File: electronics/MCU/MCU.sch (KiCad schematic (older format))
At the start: 42 parts, among them J1 UART, J10 Conn_01x09, J11 Button, J12 Power, J2 Conn_01x01, J3 Conn_01x01, J4 Conn_01x01, J5 Conn_01x01, J6 Conn_01x01, J7 Conn_01x01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

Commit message: Relay board ready, ESP3266 redesign (GPIO16 instead of GPIO0)
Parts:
- removed C2: 100n, Capacitor_SMD:C_1206_3216Metric_Pad1.42x1.75mm_HandSolder, symbol Device:C_Small
- removed SW1: Flash, Button_Switch_SMD:SW_SPST_SKQG_WithStem, symbol Switch:SW_Push
- R13: value 1k -> 10k
- R3: value 10k -> 3.3k
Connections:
- net GPIO0: now also J11.2 (Pin_2); no longer Q2.1 (G)
- net RST: now reaches R1.2, SW2.1, U1.1 (REST)
- net GPIO16: now reaches R13.2, U1.4 (GPIO16)
- net GPIO16: now also Q2.1 (G); no longer J11.2 (Pin_2)
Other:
- moved on the sheet: J11, J5, Q5, R1, R13, R2, R8, SW2

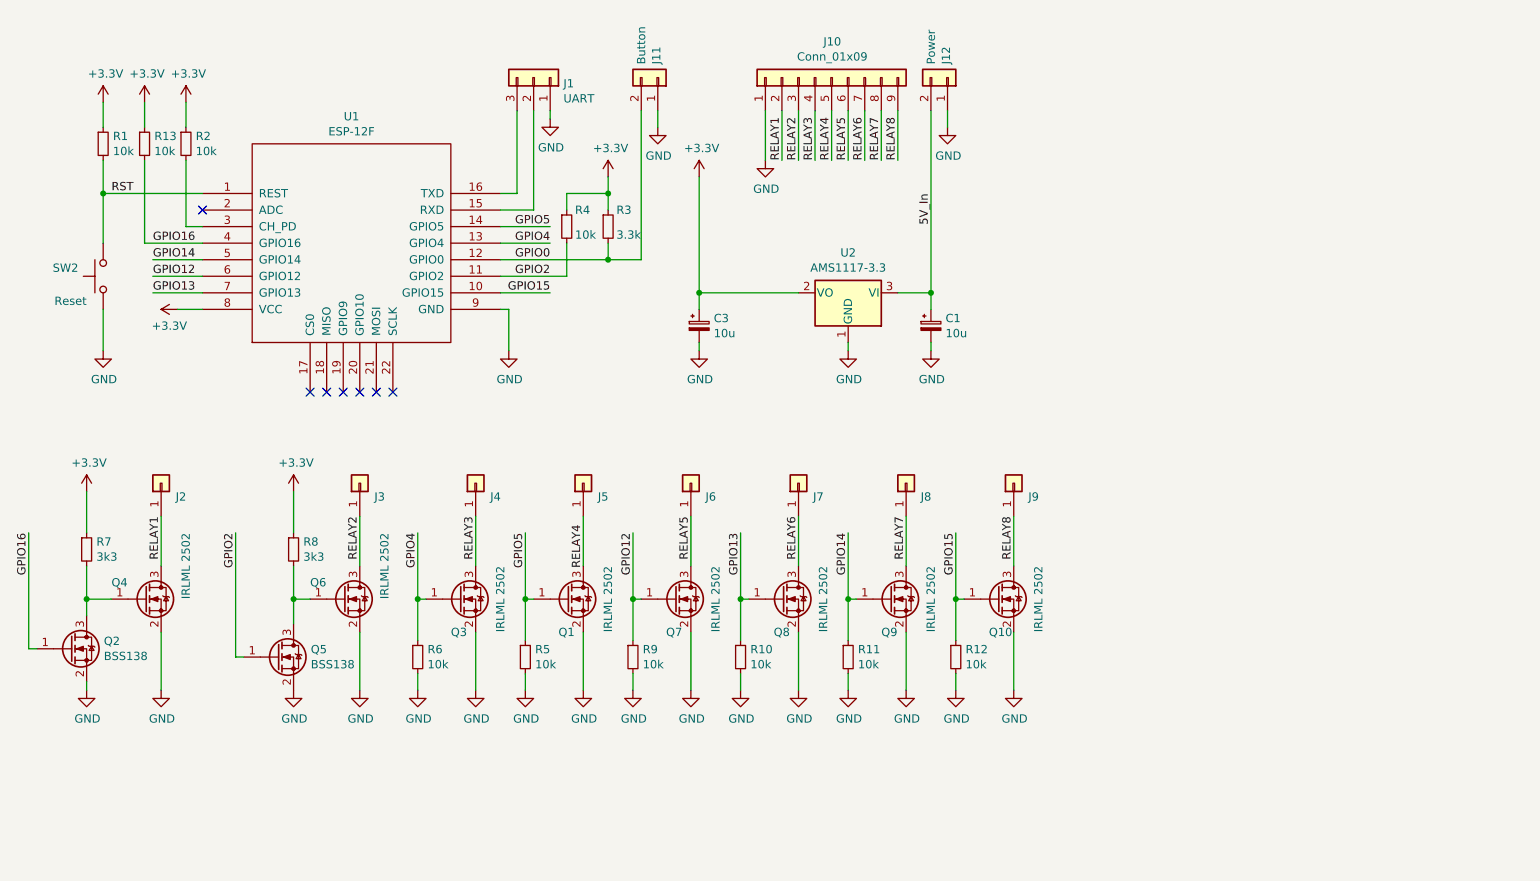
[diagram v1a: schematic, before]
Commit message: MCU: GPIO3 instead if GPIO2
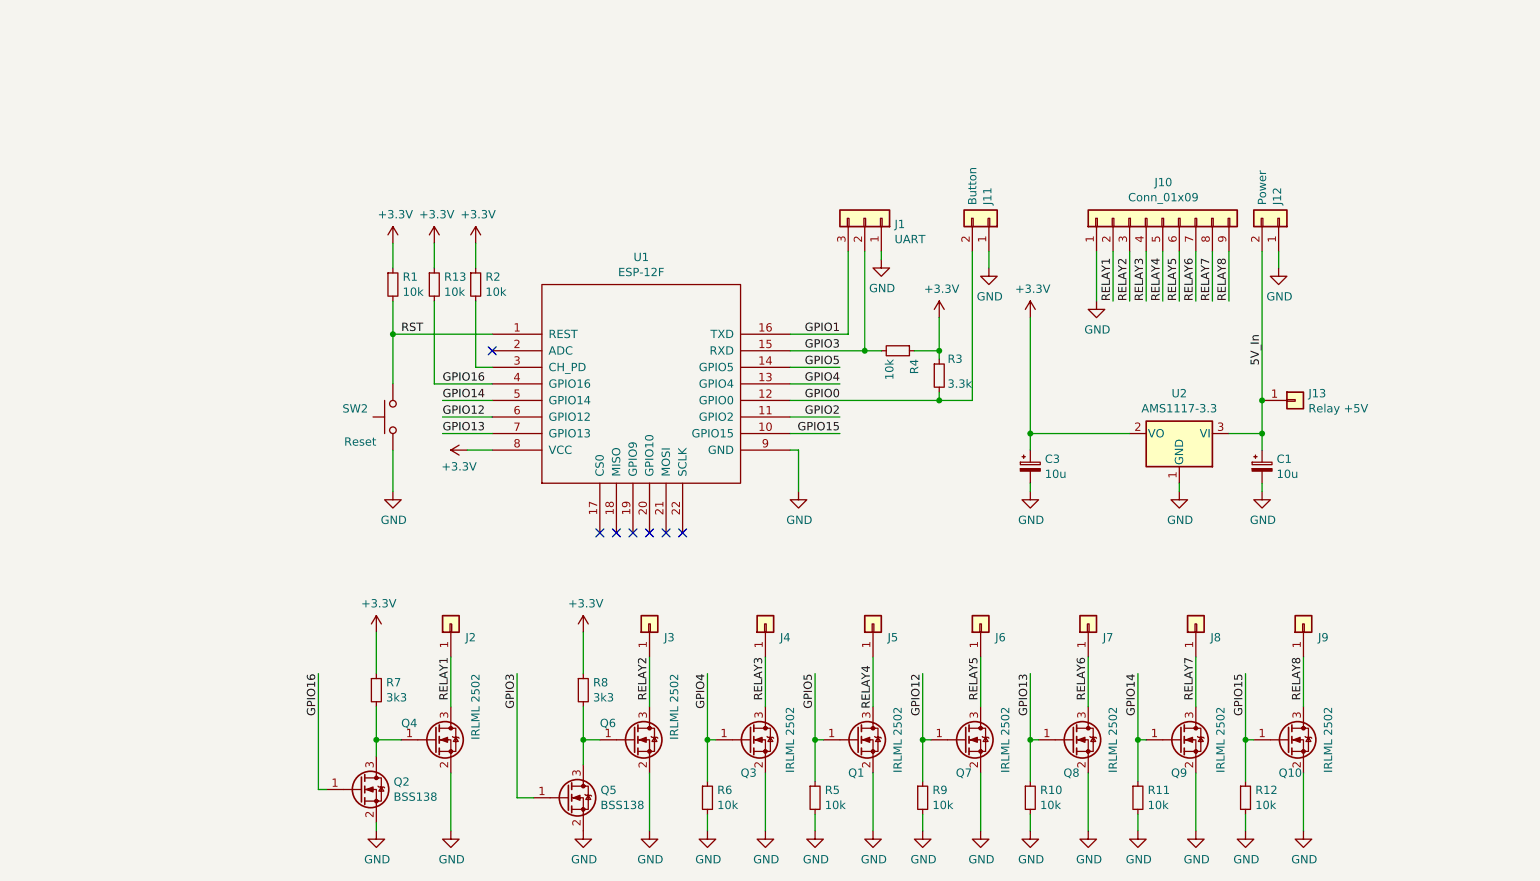
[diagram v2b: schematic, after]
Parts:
- added J13: Relay +5V, Connector_Wire:SolderWire-0.5sqmm_1x01_D0.9mm_OD2.1mm, symbol Connector_Generic:Conn_01x01
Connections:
- net 5V_In: now also J13.1 (Pin_1)
- net GPIO2: no longer Q5.1 (G), R4.2
- net GPIO3: now reaches J1.2 (Pin_2), U1.15 (RXD)
- net GPIO3: now also Q5.1 (G), R4.2
- net GPIO1: now reaches J1.3 (Pin_3), U1.16 (TXD)
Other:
- moved on the sheet: C1, C3, J1, J10, J11, J12, J2, J3, J4, J5, J6, J7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

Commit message: Small PCB modifications, esphome config added
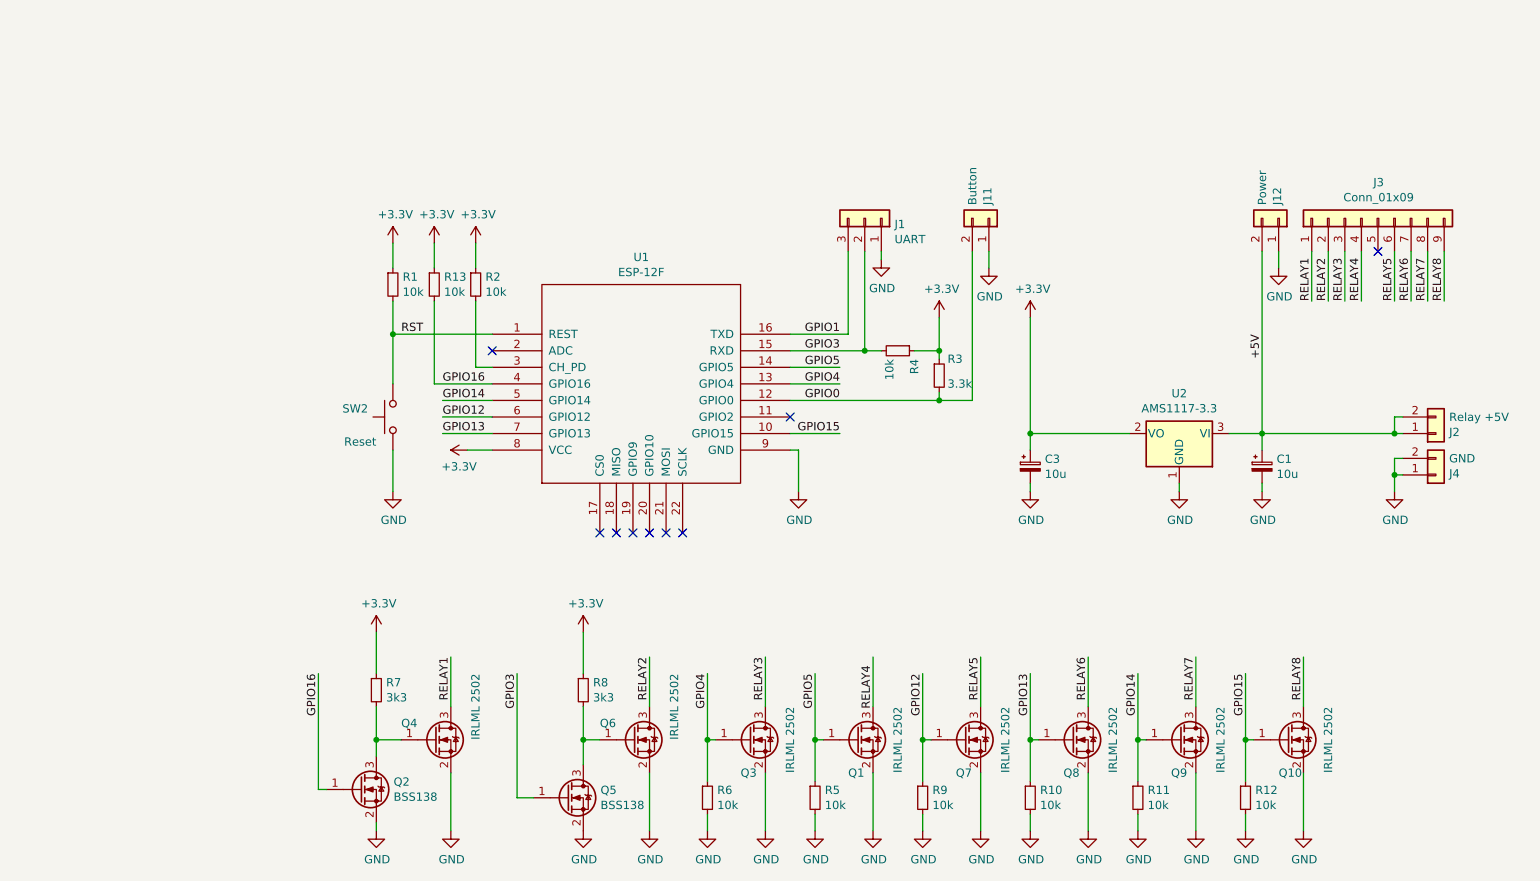
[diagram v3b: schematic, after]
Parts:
- removed J10: Conn_01x09, Connector_PinHeader_2.54mm:PinHeader_1x09_P2.54mm_Vertical, symbol Connector_Generic:Conn_01x09
- removed J13: Relay +5V, Connector_Wire:SolderWire-0.5sqmm_1x01_D0.9mm_OD2.1mm, symbol Connector_Generic:Conn_01x01
- removed J2, J3, J4, J5, J6, J7, J8, J9: Conn_01x01, Connector_Wire:SolderWirePad_1x01_SMD_1x2mm, symbol Connector_Generic:Conn_01x01
- added J2: Relay +5V, Connector_PinHeader_2.54mm:PinHeader_1x02_P2.54mm_Vertical, symbol Connector_Generic:Conn_01x02
- added J3: Conn_01x09, Connector_PinHeader_2.54mm:PinHeader_1x09_P2.54mm_Vertical, symbol Connector_Generic:Conn_01x09
- added J4: GND, Connector_PinHeader_2.54mm:PinHeader_1x02_P2.54mm_Vertical, symbol Connector_Generic:Conn_01x02
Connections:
- net GND: now also J4.1 (Pin_1), J4.2 (Pin_2)
- net RELAY1: now also J3.1 (Pin_1)
- net RELAY2: now also J3.2 (Pin_2)
- net RELAY3: now also J3.3 (Pin_3)
- net RELAY4: now also J3.4 (Pin_4)
- net RELAY5: now also J3.6 (Pin_6)
- net RELAY6: now also J3.7 (Pin_7)
- net RELAY7: now also J3.8 (Pin_8)
- net RELAY8: now also J3.9 (Pin_9)
- net 5V_In renamed +5V
- net +5V: now also J2.1 (Pin_1), J2.2 (Pin_2)
- net GPIO2: no longer names the net of U1.11 (GPIO2)
- no-connect marks 7 -> 9
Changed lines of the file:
@@
 Wire Wire Line
 	5200 2850 6100 2850
-Text Label 5500 2850 2    50   ~ 0
-GPIO0
 $Comp
 L Device:R_Small R7
@@
 Text Label 4350 4400 3    50   ~ 0
 RELAY2
-Text Label 5500 2950 2    50   ~ 0
-GPIO2
 $Comp
 L power:GND #PWR0107
@@
 	1    0    0    -1
 $EndComp
-$Comp
-L Connector_Generic:Conn_01x01 J2
-U 1 1 608085B0
-P 3150 4200
-F 0 "J2" V 3068 4112 50  0000 R CNN
-F 1 "Conn_01x01" V 3023 4112 50  0001 R CNN
-F 2 "Connector_Wire:SolderWirePad_1x01_SMD_1x2mm" H 3150 4200 50  0001 C CNN
-F 3 "~" H 3150 4200 50  0001 C CNN
-	1    3150 4200
-	0    -1   -1   0
-$EndComp
 Wire Wire Line
 	4350 4700 4350 4400
-$Comp
-L Connector_Generic:Conn_01x01 J3
-U 1 1 60809E77
-P 4350 4200
-F 0 "J3" V 4268 4112 50  0000 R CNN
-F 1 "Conn_01x01" V 4223 4112 50  0001 R CNN
-F 2 "Connector_Wire:SolderWirePad_1x01_SMD_1x2mm" H 4350 4200 50  0001 C CNN
-F 3 "~" H 4350 4200 50  0001 C CNN
-	1    4350 4200
-	0    -1   -1   0
-$EndComp
-$Comp
-L Connector_Generic:Conn_01x01 J4
-U 1 1 6080A4B7
-P 5050 4200
-F 0 "J4" V 4968 4112 50  0000 R CNN
-F 1 "Conn_01x01" V 4923 4112 50  0001 R CNN
-F 2 "Connector_Wire:SolderWirePad_1x01_SMD_1x2mm" H 5050 4200 50  0001 C CNN
-F 3 "~" H 5050 4200 50  0001 C CNN
-	1    5050 4200
-	0    -1   -1   0
-$EndComp
-$Comp
-L Connector_Generic:Conn_01x01 J5
-U 1 1 6080AAE4
-P 5700 4200
-F 0 "J5" V 5618 4112 50  0000 R CNN
-F 1 "Conn_01x01" V 5573 4112 50  0001 R CNN
-F 2 "Connector_Wire:SolderWirePad_1x01_SMD_1x2mm" H 5700 4200 50  0001 C CNN
-F 3 "~" H 5700 4200 50  0001 C CNN
-	1    5700 4200
-	0    -1   -1   0
-$EndComp
-$Comp
-L Connector_Generic:Conn_01x01 J6
-U 1 1 6080B190
-P 6350 4200
-F 0 "J6" V 6268 4112 50  0000 R CNN
-F 1 "Conn_01x01" V 6223 4112 50  0001 R CNN
-F 2 "Connector_Wire:SolderWirePad_1x01_SMD_1x2mm" H 6350 4200 50  0001 C CNN
-F 3 "~" H 6350 4200 50  0001 C CNN
-	1    6350 4200
-	0    -1   -1   0
-$EndComp
-$Comp
-L Connector_Generic:Conn_01x01 J7
-U 1 1 6080B814
-P 7000 4200
-F 0 "J7" V 6918 4112 50  0000 R CNN
-F 1 "Conn_01x01" V 6873 4112 50  0001 R CNN
-F 2 "Connector_Wire:SolderWirePad_1x01_SMD_1x2mm" H 7000 4200 50  0001 C CNN
-F 3 "~" H 7000 4200 50  0001 C CNN
-	1    7000 4200
-	0    -1   -1   0
-$EndComp
-$Comp
-L Connector_Generic:Conn_01x01 J8
-U 1 1 6080BE94
-P 7650 4200
-F 0 "J8" V 7568 4112 50  0000 R CNN
-F 1 "Conn_01x01" V 7523 4112 50  0001 R CNN
-F 2 "Connector_Wire:SolderWirePad_1x01_SMD_1x2mm" H 7650 4200 50  0001 C CNN
-F 3 "~" H 7650 4200 50  0001 C CNN
-	1    7650 4200
-	0    -1   -1   0
-$EndComp
-$Comp
-L Connector_Generic:Conn_01x01 J9
-U 1 1 6080C4EB
-P 8300 4200
-F 0 "J9" V 8218 4112 50  0000 R CNN
-F 1 "Conn_01x01" V 8173 4112 50  0001 R CNN
-F 2 "Connector_Wire:SolderWirePad_1x01_SMD_1x2mm" H 8300 4200 50  0001 C CNN
-F 3 "~" H 8300 4200 50  0001 C CNN
-	1    8300 4200
-	0    -1   -1   0
-$EndComp
-$Comp
-L Connector_Generic:Conn_01x09 J10
-U 1 1 60824243
-P 7450 1750
-F 0 "J10" V 7667 1746 50  0000 C CNN
-F 1 "Conn_01x09" V 7576 1746 50  0000 C CNN
-F 2 "Connector_PinHeader_2.54mm:PinHeader_1x09_P2.54mm_Vertical" H 7450 1750 50  0001 C CNN
-F 3 "~" H 7450 1750 50  0001 C CNN
-	1    7450 1750
-	0    -1   -1   0
-$EndComp
-Wire Wire Line
-	7050 1950 7050 2250
-Wire Wire Line
-	7150 1950 7150 2250
-Wire Wire Line
-	7250 1950 7250 2250
-Wire Wire Line
-	7350 1950 7350 2250
-Wire Wire Line
-	7450 1950 7450 2250
-Wire Wire Line
-	7550 1950 7550 2250
-Wire Wire Line
-	7650 1950 7650 2250
-Wire Wire Line
-	7750 1950 7750 2250
-Wire Wire Line
-	7850 1950 7850 2250
-Text Label 7150 2250 1    50   ~ 0
-RELAY1
-Text Label 7250 2250 1    50   ~ 0
-RELAY2
-Text Label 7350 2250 1    50   ~ 0
-RELAY3
-Text Label 7450 2250 1    50   ~ 0
-RELAY4
-Text Label 7550 2250 1    50   ~ 0
-RELAY5
-Text Label 7650 2250 1    50   ~ 0
-RELAY6
-Text Label 7750 2250 1    50   ~ 0
-RELAY7
-Text Label 7850 2250 1    50   ~ 0
-RELAY8
-$Comp
-L power:GND #PWR0130
-U 1 1 6084ABDB
-P 7050 2250
-F 0 "#PWR0130" H 7050 2000 50  0001 C CNN
-F 1 "GND" H 7055 2077 50  0000 C CNN
-F 2 "" H 7050 2250 50  0001 C CNN
-F 3 "" H 7050 2250 50  0001 C CNN
-	1    7050 2250
-	1    0    0    -1
-$EndComp
 Wire Wire Line
 	2800 2250 2800 2450
@@
 	8150 2050 8150 1950
 Wire Wire Line
-	8050 1950 8050 2850
-Wire Wire Line
 	8050 3050 7850 3050
 Wire Wire Line
@@
 	7550 3400 7550 3350
 Text Label 8050 2450 3    50   ~ 0
-5V_In
++5V
 $Comp
 L Device:CP_Small C3
@@
 GPIO1
 Wire Wire Line
-	5200 2950 5500 2950
-Wire Wire Line
 	6100 2350 6100 2550
 Wire Wire Line
@@
 Wire Wire Line
 	3550 4500 3550 5250
-$Comp
-L Connector_Generic:Conn_01x01 J13
-U 1 1 6091A2E0
-P 8250 2850
-F 0 "J13" H 8330 2892 50  0000 L CNN
-F 1 "Relay +5V" H 8330 2801 50  0000 L CNN
-F 2 "Connector_Wire:SolderWire-0.5sqmm_1x01_D0.9mm_OD2.1mm" H 8250 2850 50  0001 C CNN
-F 3 "~" H 8250 2850 50  0001 C CNN
-	1    8250 2850
-	1    0    0    -1
-$EndComp
-Connection ~ 8050 2850
-Wire Wire Line
-	8050 2850 8050 3050
+Text Label 5500 2850 2    50   ~ 0
+GPIO0
+NoConn ~ 5200 2950
+Wire Wire Line
+	8450 1950 8450 2250
+Wire Wire Line
+	8550 1950 8550 2250
+Wire Wire Line
+	8650 1950 8650 2250
+Wire Wire Line
+	8850 1950 8850 2250
+Wire Wire Line
+	8950 1950 8950 2250
+Wire Wire Line
+	9050 1950 9050 2250
+Wire Wire Line
+	9150 1950 9150 2250
+Text Label 8350 2250 1    50   ~ 0
+RELAY1
+Text Label 8450 2250 1    50   ~ 0
+RELAY2
+Text Label 8550 2250 1    50   ~ 0
+RELAY3
+Text Label 8650 2250 1    50   ~ 0
+RELAY4
+Text Label 8850 2250 1    50   ~ 0
+RELAY5
+Text Label 8950 2250 1    50   ~ 0
+RELAY6
+Text Label 9050 2250 1    50   ~ 0
+RELAY7
+Text Label 9150 2250 1    50   ~ 0
+RELAY8
+$Comp
+L Connector_Generic:Conn_01x09 J3
+U 1 1 6082EAF2
+P 8750 1750
+F 0 "J3" V 8967 1746 50  0000 C CNN
+F 1 "Conn_01x09" V 8876 1746 50  0000 C CNN
+F 2 "Connector_PinHeader_2.54mm:PinHeader_1x09_P2.54mm_Vertical" H 8750 1750 50  0001 C CNN
+F 3 "~" H 8750 1750 50  0001 C CNN
+	1    8750 1750
+	0    -1   -1   0
+$EndComp
+Wire Wire Line
+	8050 1950 8050 3050
+Wire Wire Line
+	8350 1950 8350 2250
+NoConn ~ 8750 1950
+$Comp
+L Connector_Generic:Conn_01x02 J2
+U 1 1 6090F57A
+P 9100 3050
+F 0 "J2" H 9180 3042 50  0000 L CNN
+F 1 "Relay +5V" H 9180 2951 50  0000 L CNN
+F 2 "Connector_PinHeader_2.54mm:PinHeader_1x02_P2.54mm_Vertical" H 9100 3050 50  0001 C CNN
+F 3 "~" H 9100 3050 50  0001 C CNN
+	1    9100 3050
+	1    0    0    1
+$EndComp
+$Comp
+L Connector_Generic:Conn_01x02 J4
+U 1 1 609101A1
+P 9100 3300
+F 0 "J4" H 9180 3292 50  0000 L CNN
+F 1 "GND" H 9180 3201 50  0000 L CNN
+F 2 "Connector_PinHeader_2.54mm:PinHeader_1x02_P2.54mm_Vertical" H 9100 3300 50  0001 C CNN
+F 3 "~" H 9100 3300 50  0001 C CNN
+	1    9100 3300
+	1    0    0    1
+$EndComp
+Wire Wire Line
+	8900 2950 8850 2950
+Wire Wire Line
+	8850 2950 8850 3050
+Wire Wire Line
+	8850 3050 8900 3050
+Wire Wire Line
+	8900 3200 8850 3200
+Wire Wire Line
+	8850 3200 8850 3300
+Wire Wire Line
+	8850 3300 8900 3300
+Wire Wire Line
+	8850 3300 8850 3400
+Connection ~ 8850 3300
+$Comp
+L power:GND #PWR01
+U 1 1 60921387
+P 8850 3400
+F 0 "#PWR01" H 8850 3150 50  0001 C CNN
+F 1 "GND" H 8855 3227 50  0000 C CNN
+F 2 "" H 8850 3400 50  0001 C CNN
+F 3 "" H 8850 3400 50  0001 C CNN
+	1    8850 3400
+	1    0    0    -1
+$EndComp
+Wire Wire Line
+	8050 3050 8850 3050
+Connection ~ 8850 3050
 $EndSCHEMATC
